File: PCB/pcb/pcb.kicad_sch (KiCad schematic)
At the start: 8 parts, among them J1 Reed, J2 Button, J3 LED, J4 Servo Signal, U1 NodeMCU1.0(ESP-12E), U2 ACS712xLCTR-30A

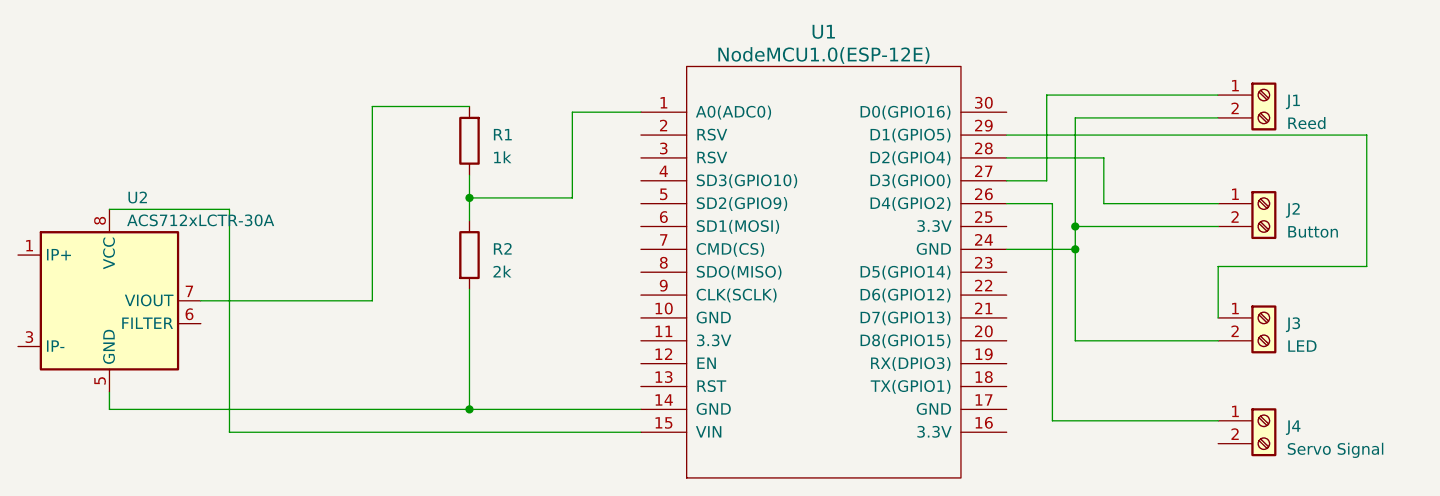
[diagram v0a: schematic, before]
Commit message: updated the PCB
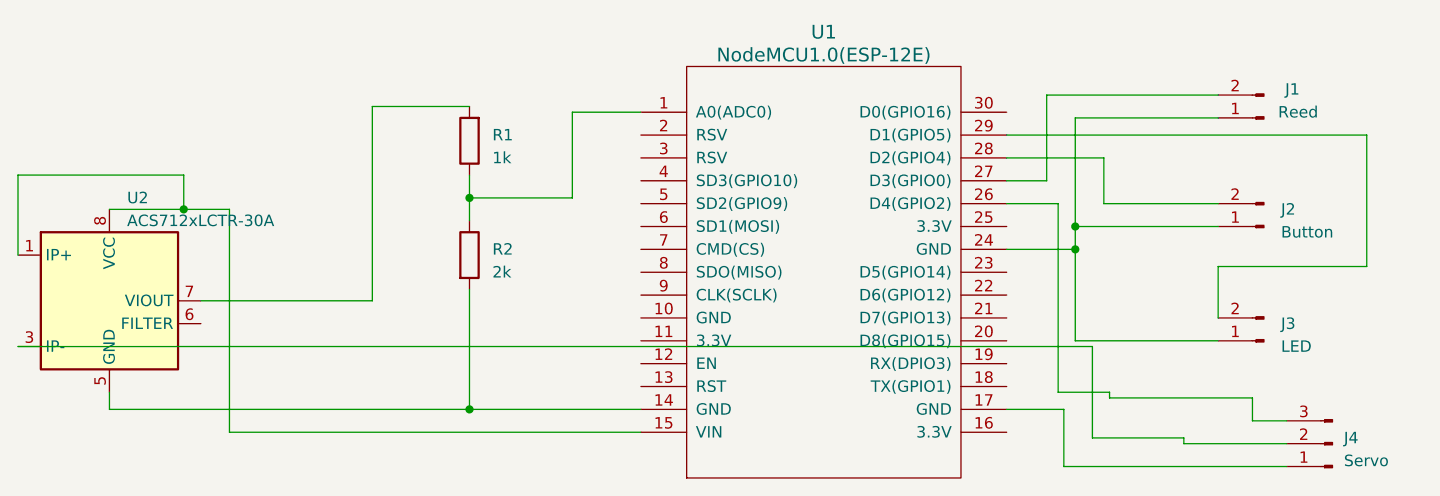
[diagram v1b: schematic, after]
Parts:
- removed J1: Reed, TerminalBlock_4Ucon:TerminalBlock_4Ucon_1x02_P3.50mm_Horizontal, symbol Connector:Screw_Terminal_01x02
- removed J2: Button, TerminalBlock_4Ucon:TerminalBlock_4Ucon_1x02_P3.50mm_Horizontal, symbol Connector:Screw_Terminal_01x02
- removed J3: LED, TerminalBlock_4Ucon:TerminalBlock_4Ucon_1x02_P3.50mm_Horizontal, symbol Connector:Screw_Terminal_01x02
- removed J4: Servo Signal, TerminalBlock_4Ucon:TerminalBlock_4Ucon_1x02_P3.50mm_Horizontal, symbol Connector:Screw_Terminal_01x02
- added J1: Reed, Connector_JST:JST_EH_B2B-EH-A_1x02_P2.50mm_Vertical, symbol Connector:Conn_01x02_Pin
- added J2: Button, Connector_JST:JST_EH_B2B-EH-A_1x02_P2.50mm_Vertical, symbol Connector:Conn_01x02_Pin
- added J3: LED, Connector_JST:JST_EH_B2B-EH-A_1x02_P2.50mm_Vertical, symbol Connector:Conn_01x02_Pin
- added J4: Servo, Connector_JST:JST_EH_B3B-EH-A_1x03_P2.50mm_Vertical, symbol Connector:Conn_01x03_Pin
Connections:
- net at U1.29 (D1(GPIO5)): now also J3.2 (Pin_2)
- net at U1.24 (GND): now also J1.1 (Pin_1), J2.1 (Pin_1), J3.1 (Pin_1)
- net at U1.27 (D3(GPIO0)): now also J1.2 (Pin_2)
- net at U1.28 (D2(GPIO4)): now also J2.2 (Pin_2)
- net at U1.15 (VIN), U2.8 (VCC): now also U2.1 (IP+), U2.2 (IP+)
- net at U1.17 (GND): now also J4.1 (Pin_1)
- net at U1.26 (D4(GPIO2)): now also J4.3 (Pin_3)
- net at U2.3 (IP-), U2.4 (IP-): now also J4.2 (Pin_2)

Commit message: finished PCB design
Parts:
- J1, J2, J3: footprint Connector_JST:JST_EH_B2B-EH-A_1x02_P2.50mm_Vertical -> Connector_PinHeader_2.54mm:PinHeader_1x02_P2.54mm_Vertical
- J4: footprint Connector_JST:JST_EH_B3B-EH-A_1x03_P2.50mm_Vertical -> Connector_PinHeader_2.54mm:PinHeader_1x03_P2.54mm_Vertical
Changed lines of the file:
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@@
       (effects (font (size 1.27 1.27)) (justify right))
     )
-    (property "Footprint" "Connector_JST:JST_EH_B2B-EH-A_1x02_P2.50mm_Vertical" (at 199.39 84.455 0)
+    (property "Footprint" "Connector_PinHeader_2.54mm:PinHeader_1x02_P2.54mm_Vertical" (at 199.39 84.455 0)
       (effects (font (size 1.27 1.27)) hide)
     )
@@
       (effects (font (size 1.27 1.27)))
     )
-    (property "Footprint" "Connector_JST:JST_EH_B2B-EH-A_1x02_P2.50mm_Vertical" (at 199.39 72.39 0)
+    (property "Footprint" "Connector_PinHeader_2.54mm:PinHeader_1x02_P2.54mm_Vertical" (at 199.39 72.39 0)
       (effects (font (size 1.27 1.27)) hide)
     )
@@
       (effects (font (size 1.27 1.27)) (justify right))
     )
-    (property "Footprint" "Connector_JST:JST_EH_B3B-EH-A_1x03_P2.50mm_Vertical" (at 207.01 108.585 0)
+    (property "Footprint" "Connector_PinHeader_2.54mm:PinHeader_1x03_P2.54mm_Vertical" (at 207.01 108.585 0)
       (effects (font (size 1.27 1.27)) hide)
     )
@@
       (effects (font (size 1.27 1.27)) (justify right))
     )
-    (property "Footprint" "Connector_JST:JST_EH_B2B-EH-A_1x02_P2.50mm_Vertical" (at 199.39 97.155 0)
-      (effects (font (size 1.27 1.27)) hide)
-    )
+    (property "Footprint" "Connector_PinHeader_2.54mm:PinHeader_1x02_P2.54mm_Vertical" (at 199.39 97.155 0)
+      (effects (font (size 1.27 1.27)) hide)
+    )
